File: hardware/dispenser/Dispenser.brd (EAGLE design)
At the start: 73.7 x 75.6 mm, 59 parts, among them J1 AVR_Prog, J2 RJ45-8PTH, Q1 NFET-SO8, Q2 NFET, Q3 NFET, Q4 NFET, U1 ATMEGA168, U10 HALL-EFFECT, U2 OPAMP-DUAL, U3 OPTO-TLP185, U4 MPX10DP, U5 VREG-5V-LDO-AP1117SOT89-3L, U6 WS2801, U7 HALL-EFFECT, U8 HALL-EFFECT, U9 HALL-EFFECT

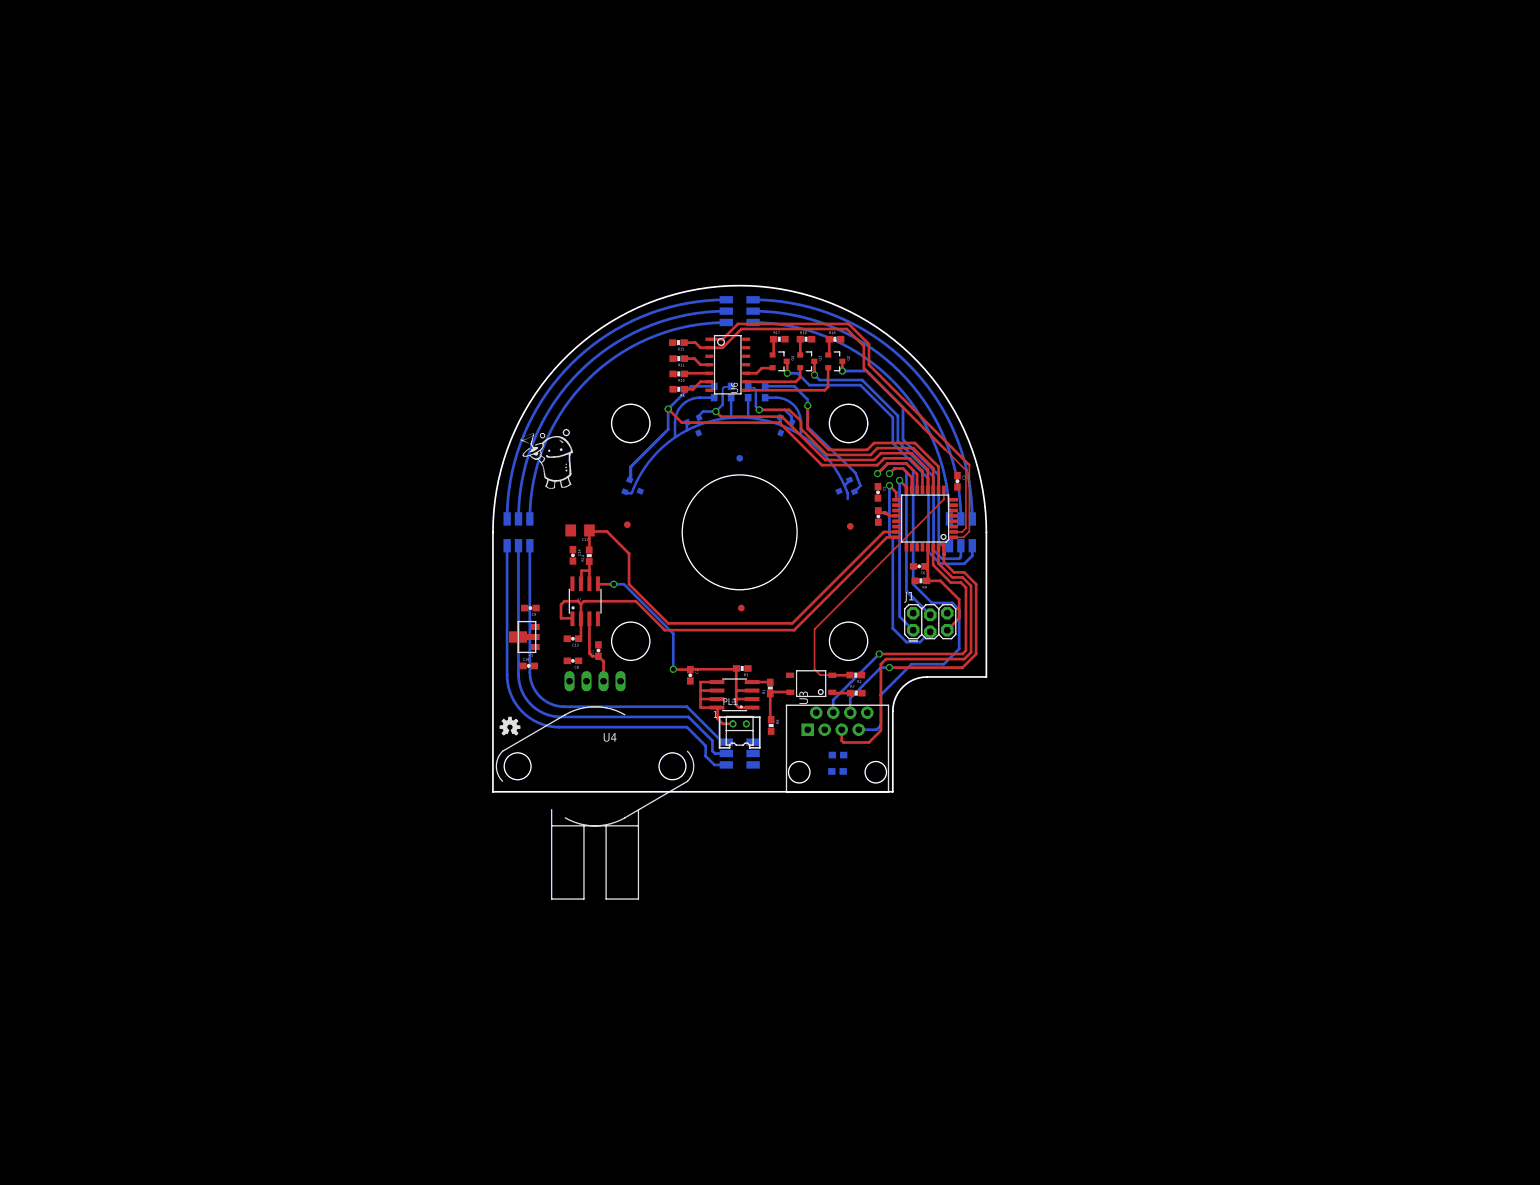
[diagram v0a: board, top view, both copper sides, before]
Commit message: Updated Router Schematic with DS1307 and Accessory Port
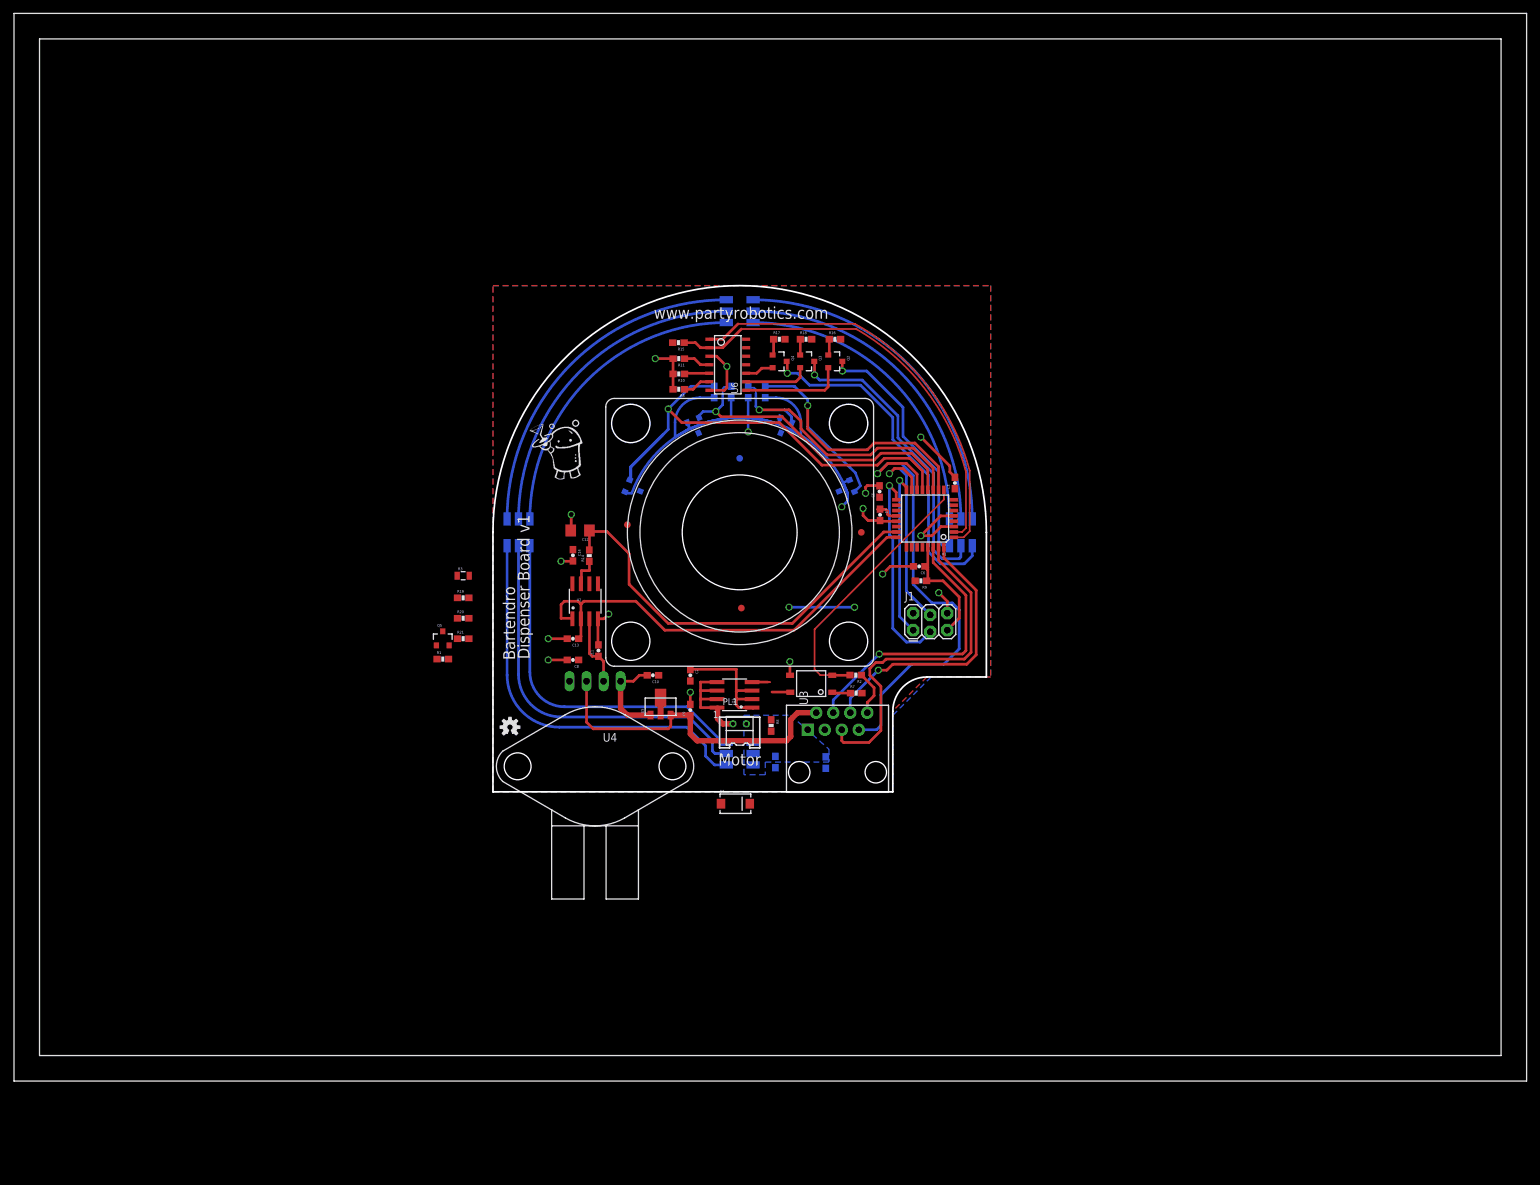
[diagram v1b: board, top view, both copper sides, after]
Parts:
- added D1: (no value), pierre:SMA-DIODE
- added Q5: MOSFET-NCHANNELSMD, SparkFun-DiscreteSemi:SOT23-3
- added R19, R20: 1k, SparkFun-Resistors:0603-RES
- added R21: 10k, SparkFun-Resistors:0603-RES
- C10: value 2.2u -> 10u
- C11, C2: value 47n -> 100n
- C12: value 100u -> 10u
- R1: value 10 -> 10k
- R14: value 10 -> 1k
- R15: value 2.2k -> 1k
- R3: value 0.1 -> 0.2; device SparkFun-Resistors:0603-RES -> SparkFun-Resistors:0805
- R8: value 10k -> 330
- moved R1 49.1 mm to (-7.49, 19.8), turned to 0 degrees
- moved R3 43.9 mm to (-4.45, 32.3), turned to 0 degrees
- moved C9 28.3 mm to (29.5, 12.2), turned to 90 degrees
- moved U5 22.5 mm to (25.0, 12.7), turned to 0 degrees
- moved C10 18.6 mm to (23.9, 17.4), turned to 180 degrees
- moved C1 9.38 mm to (42.2, 4.45), turned to 270 degrees
- moved FRAME3 2.74 mm to (18.4, 84.2)
- moved C4 2.14 mm to (49.7, 4.37), turned to 270 degrees
- moved JP7 1.88 mm to (55.0, 38.7)
- moved C3 0.46 mm to (69.0, 46.1), turned to 90 degrees
- moved C7 0.36 mm to (57.8, 41.4)
- moved C5 0.26 mm to (57.7, 44.8), turned to 90 degrees
- moved C8 0.13 mm to (11.9, 19.7)
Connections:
- new net N$10: C2.1, R20.1, R21.2, U2.6
- new net N$11: R19.1, U2.5
- net 3.3V: now also R1.2; no longer U4.3
- net 5V: now also U4.3
- net CURRENT_SENSE: now also R19.2; no longer C2.1, U2.5
- net GND: now also Q5.2, R20.2; no longer C2.2
- net MOT_B: now also D1.A
- net MOT_CUR: now also C2.2, R21.1; no longer U2.6
- net N$31: now also Q5.1; no longer R1.1
- net N$9: now also Q5.3, R1.1; no longer R1.2
- net VIN: now also D1.C
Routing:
- net GND: track 0.00 -> 94.6 mm, vias 0 -> 15
- net 5V: track 0.00 -> 49.1 mm
- net 3.3V: track 62.0 -> 98.7 mm, vias 0 -> 4
- net CURRENT_SENSE: track 42.0 -> 19.8 mm, vias 2 -> 0
- net N$31: track 7.04 -> 2.92 mm
- net MOT_CUR: track 6.53 -> 4.58 mm
- net TX: track 51.0 -> 52.1 mm
- net N$29: track 1.02 -> 0.00 mm
- net RX: track 43.1 -> 42.2 mm
- net N$1: track 3.01 -> 3.83 mm
- net RESET: track 42.5 -> 41.7 mm
- net LED_CLK: track 62.9 -> 62.3 mm
- added copper zone on layer 1, net 3.3V
- added copper zone on layer 16, net GND
- added copper zone on layer 16, net VIN
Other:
- board text added: "Bartendro"
- board text added: "Dispenser Board v1"
- board text added: "Motor"
- board text added: "www.partyrobotics.com"

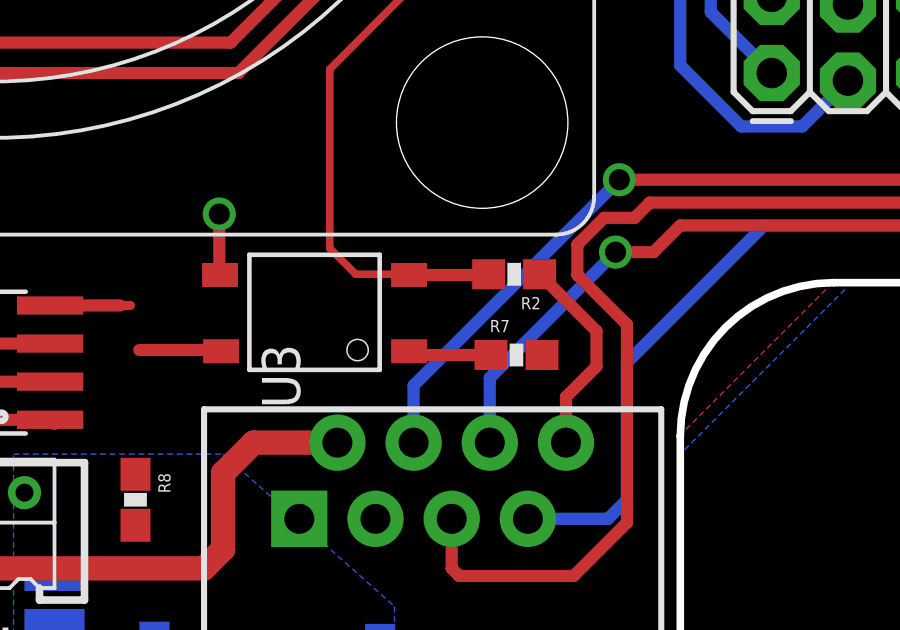
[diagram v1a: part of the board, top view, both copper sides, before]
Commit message: Updated inputs to opto-isolator
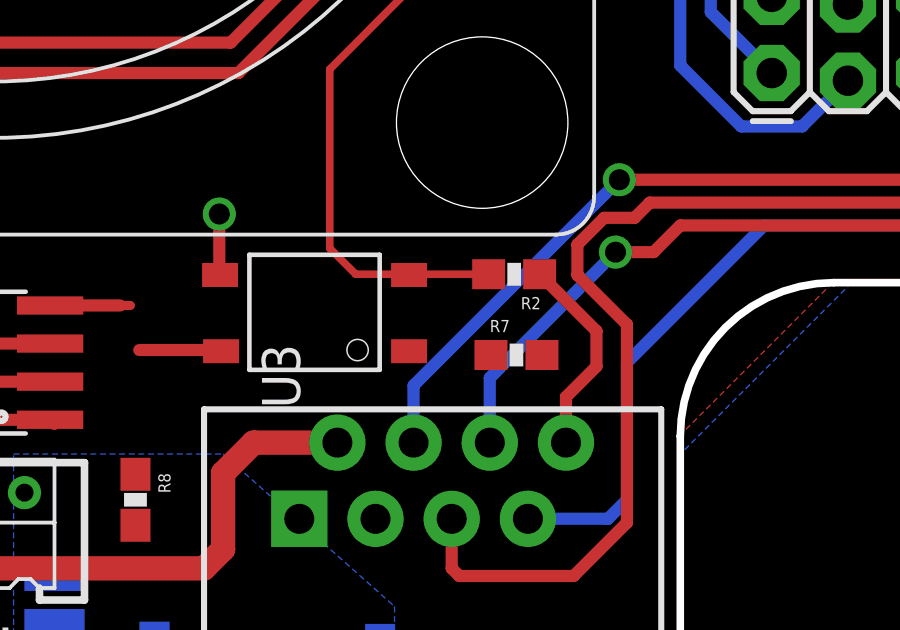
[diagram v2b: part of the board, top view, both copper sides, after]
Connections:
- removed net N$35: R7.1, U3.1
- new net N$15: R7.2, U3.3
- net 3.3V: no longer R7.2
- net GND: now also R7.1
- net MOT_CTL: now also U3.1; no longer U3.3
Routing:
- net N$35: track 2.78 -> 0.00 mm
- net MOT_CTL: track 43.1 -> 40.5 mm
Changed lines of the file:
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@@
 <contactref element="R20" pad="2"/>
 <contactref element="Q5" pad="2"/>
-<wire x1="-3.595" y1="25.908" x2="-5.345" y2="32.258" width="0" layer="19" extent="1-1"/>
+<contactref element="R7" pad="1"/>
+<wire x1="68.8086" y1="41.1924" x2="68.961" y2="46.951" width="0" layer="19" extent="1-1"/>
+<wire x1="60.2234" y1="40.3924" x2="63.881" y2="38.227" width="0" layer="19" extent="1-1"/>
+<wire x1="55.626" y1="44.577" x2="55.2568" y2="42.3028" width="0" layer="19" extent="1-1"/>
+<wire x1="51.663334375" y1="44.867246875" x2="55.626" y2="44.577" width="0" layer="19" extent="16-16"/>
+<wire x1="62.777" y1="33.655" x2="63.881" y2="38.227" width="0" layer="19" extent="1-1"/>
+<wire x1="66.548" y1="29.718" x2="62.777" y2="33.655" width="0" layer="19" extent="1-1"/>
+<wire x1="42.96225" y1="53.56833125" x2="51.663334375" y2="44.867246875" width="0" layer="19" extent="16-16"/>
+<wire x1="34.925" y1="60.325" x2="42.96225" y2="53.56833125" width="0" layer="19" extent="1-16"/>
+<wire x1="26.8868" y1="64.6684" x2="32.302" y2="65.024" width="0" layer="19" extent="1-1"/>
+<wire x1="30.697753125" y1="53.56833125" x2="32.302" y2="59.944" width="0" layer="19" extent="1-16"/>
+<wire x1="21.99666875" y1="44.867246875" x2="30.697753125" y2="53.56833125" width="0" layer="19" extent="16-16"/>
+<wire x1="11.684" y1="41.402" x2="21.99666875" y2="44.867246875" width="0" layer="19" extent="16-16"/>
+<wire x1="11.938" y1="34.456" x2="11.6048" y2="39.0144" width="0" layer="19" extent="1-1"/>
+<wire x1="15.6718" y1="25.8318" x2="11.899" y2="34.417" width="0" layer="19" extent="1-1"/>
+<wire x1="11.088" y1="22.86" x2="15.6718" y2="22.0082" width="0" layer="19" extent="1-1"/>
+<wire x1="11.088" y1="19.685" x2="11.088" y2="22.86" width="0" layer="19" extent="1-1"/>
+<wire x1="19.05" y1="16.51" x2="15.748" y2="21.932" width="0" layer="19" extent="1-1"/>
+<wire x1="29.464" y1="13.042" x2="23.519" y2="11.45" width="0" layer="19" extent="1-1"/>
+<wire x1="-3.595" y1="25.908" x2="8.255" y2="22.86" width="0" layer="19" extent="1-1"/>
 <wire x1="-6.543" y1="21.86" x2="-3.595" y2="25.908" width="0" layer="19" extent="1-1"/>
-<wire x1="8.255" y1="22.86" x2="-3.595" y2="25.908" width="0" layer="19" extent="1-1"/>
+<wire x1="-5.345" y1="32.258" x2="-3.595" y2="25.908" width="0" layer="19" extent="1-1"/>
+<wire x1="44.348" y1="17.399" x2="29.464" y2="14.859" width="0" layer="19" extent="1-1"/>
+<wire x1="53.379" y1="14.732" x2="44.348" y2="17.399" width="0" layer="19" extent="1-1"/>
+<wire x1="55.88" y1="13.335" x2="53.379" y2="14.732" width="0" layer="19" extent="1-1"/>
+<wire x1="49.6824" y1="3.5188" x2="55.88" y2="11.811" width="0" layer="19" extent="16-16"/>
+<wire x1="42.164" y1="3.595" x2="49.6824" y2="3.5188" width="0" layer="19" extent="16-16"/>
 </signal>
 <signal name="5V">
@@
 <wire x1="-3.595" y1="28.956" x2="29.503" y2="18.288" width="0" layer="19" extent="1-1"/>
 <wire x1="-3.545" y1="32.258" x2="-3.595" y2="28.956" width="0" layer="19" extent="1-1"/>
-</signal>
-<signal name="N$35">
-<contactref element="R7" pad="1"/>
-<contactref element="U3" pad="1"/>
-<wire x1="50.648" y1="14.859" x2="50.775" y2="14.732" width="0.4064" layer="1"/>
-<wire x1="50.775" y1="14.732" x2="53.379" y2="14.732" width="0.4064" layer="1"/>
 </signal>
 <signal name="TX">
@@
 <contactref element="C5" pad="1"/>
 <contactref element="C8" pad="1"/>
-<contactref element="R7" pad="2"/>
 <contactref element="J1" pad="2"/>
 <contactref element="R8" pad="2"/>
@@
 <wire x1="20.7264" y1="44.6024" x2="20.701" y2="44.577" width="0.4064" layer="16"/>
 <contactref element="R1" pad="2"/>
-<wire x1="12.788" y1="19.685" x2="-6.643" y2="19.812" width="0" layer="19" extent="1-1"/>
+<wire x1="47.586" y1="67.564" x2="51.904" y2="67.564" width="0" layer="19" extent="1-1"/>
+<wire x1="43.5982" y1="67.564" x2="47.586" y2="67.564" width="0" layer="19" extent="1-1"/>
+<wire x1="37.802" y1="67.564" x2="43.5982" y2="67.564" width="0" layer="19" extent="1-1"/>
+<wire x1="38.1" y1="58.84" x2="37.802" y2="67.564" width="0" layer="19" extent="1-16"/>
+<wire x1="26.836" y1="67.056" x2="30.9" y2="58.84" width="0" layer="19" extent="1-16"/>
+<wire x1="52.2732" y1="46.1518" x2="45.974" y2="53.213" width="0" layer="19" extent="16-16"/>
+<wire x1="57.7088" y1="43.981" x2="52.959" y2="43.434" width="0" layer="19" extent="1-16"/>
+<wire x1="60.2234" y1="42.7924" x2="57.7088" y2="43.981" width="0" layer="19" extent="1-1"/>
+<wire x1="68.8086" y1="41.9924" x2="60.2234" y2="42.7924" width="0" layer="19" extent="1-1"/>
+<wire x1="68.8086" y1="40.3924" x2="68.8086" y2="41.9924" width="0" layer="19" extent="1-1"/>
+<wire x1="68.961" y1="45.251" x2="68.8086" y2="41.9924" width="0" layer="19" extent="1-1"/>
+<wire x1="63.031" y1="31.496" x2="68.8086" y2="40.3924" width="0" layer="19" extent="1-1"/>
+<wire x1="62.738" y1="26.67" x2="63.031" y2="31.496" width="0" layer="19" extent="1-1"/>
+<wire x1="53.975" y1="27.559" x2="62.738" y2="26.67" width="0" layer="19" extent="1-1"/>
+<wire x1="11.938" y1="36.156" x2="19.90916875" y2="44.577" width="0" layer="19" extent="1-16"/>
+<wire x1="11.8618" y1="31.0642" x2="11.938" y2="36.156" width="0" layer="19" extent="1-1"/>
+<wire x1="12.788" y1="19.685" x2="11.8618" y2="31.0642" width="0" layer="19" extent="1-1"/>
+<wire x1="24.726" y1="17.399" x2="12.788" y2="19.685" width="0" layer="19" extent="1-1"/>
+<wire x1="25.019" y1="14.05" x2="24.726" y2="17.399" width="0" layer="19" extent="1-1"/>
+<wire x1="25.019" y1="11.75" x2="25.019" y2="14.05" width="0" layer="19" extent="1-1"/>
+<wire x1="41.529" y1="9.056" x2="25.019" y2="11.75" width="0" layer="19" extent="1-1"/>
+<wire x1="-6.643" y1="19.812" x2="12.788" y2="19.685" width="0" layer="19" extent="1-1"/>
 </signal>
 <signal name="LED_CLK">
@@
 </signal>
 <signal name="MOT_CTL">
-<contactref element="U3" pad="3"/>
 <contactref element="R2" pad="2"/>
 <contactref element="U1" pad="9"/>
 <wire x1="53.3028" y1="17.4244" x2="53.2774" y2="17.399" width="0.4064" layer="1"/>
-<wire x1="53.2774" y1="17.399" x2="50.648" y2="17.399" width="0.4064" layer="1"/>
 <wire x1="67.316" y1="45.085" x2="67.316" y2="43.6432" width="0.254" layer="1"/>
 <wire x1="53.3028" y1="17.4244" x2="48.8696" y2="17.4244" width="0.254" layer="1"/>
@@
 <wire x1="48.006" y1="18.288" x2="48.006" y2="24.257" width="0.254" layer="1"/>
 <wire x1="48.006" y1="24.257" x2="67.316" y2="43.6432" width="0.254" layer="1"/>
+<contactref element="U3" pad="1"/>
+<wire x1="50.648" y1="14.859" x2="48.8696" y2="17.4244" width="0" layer="19" extent="1-1"/>
 </signal>
 <signal name="N$6">
@@
 <wire x1="-5.295" y1="28.956" x2="15.6718" y2="31.0642" width="0" layer="19" extent="1-1"/>
 </signal>
+<signal name="N$15">
+<contactref element="R7" pad="2"/>
+<contactref element="U3" pad="3"/>
+<wire x1="50.648" y1="17.399" x2="55.079" y2="14.732" width="0" layer="19" extent="1-1"/>
+</signal>
 </signals>
